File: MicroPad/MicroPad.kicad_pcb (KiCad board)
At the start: 2 copper layers, 92 x 92 mm, 69 parts, among them J10 Conn_01x02, J11 Conn_01x02, J12 Conn_01x02, J2 USB_C_Receptacle_USB2.0_16P, J4 Programming header, J5 SPI for E-Ink Display, J6 B2B-PH-K-S (Battery), J9 Conn_01x02, SW1 RESET, SW10 SWITCH, SW11 SWITCH, SW12 SWITCH, SW13 SWITCH, SW14 SWITCH, SW15 RotaryEncoder_Switch_MP, SW2 BOOT, SW3 SWITCH, SW4 SWITCH, SW5 SWITCH, SW6 SWITCH, SW7 SWITCH, SW8 SWITCH, SW9 SWITCH, U1 BQ24075RGT, U3 ESP32-S3-WROOM-1, U5 ESD7104MUTAG, U6 AP2112K-3.3

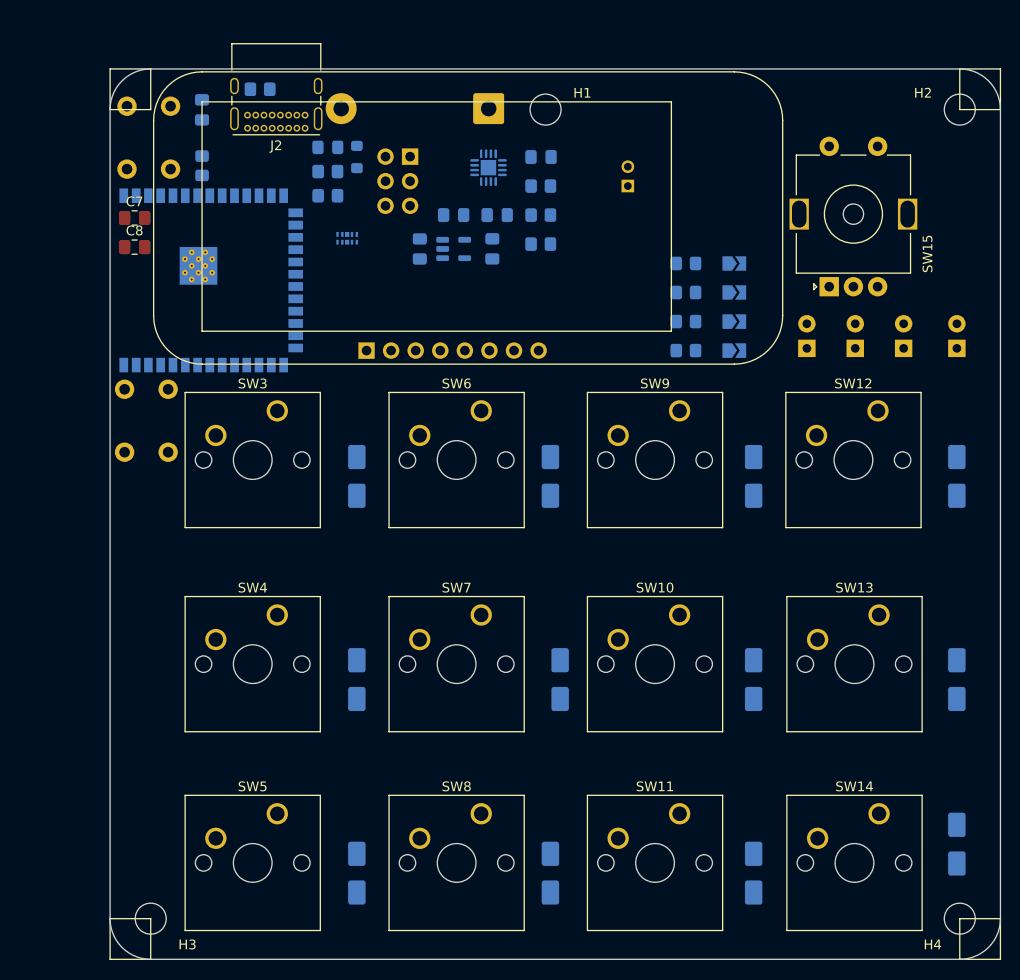
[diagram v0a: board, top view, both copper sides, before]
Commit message: new version with bigger display and one key less
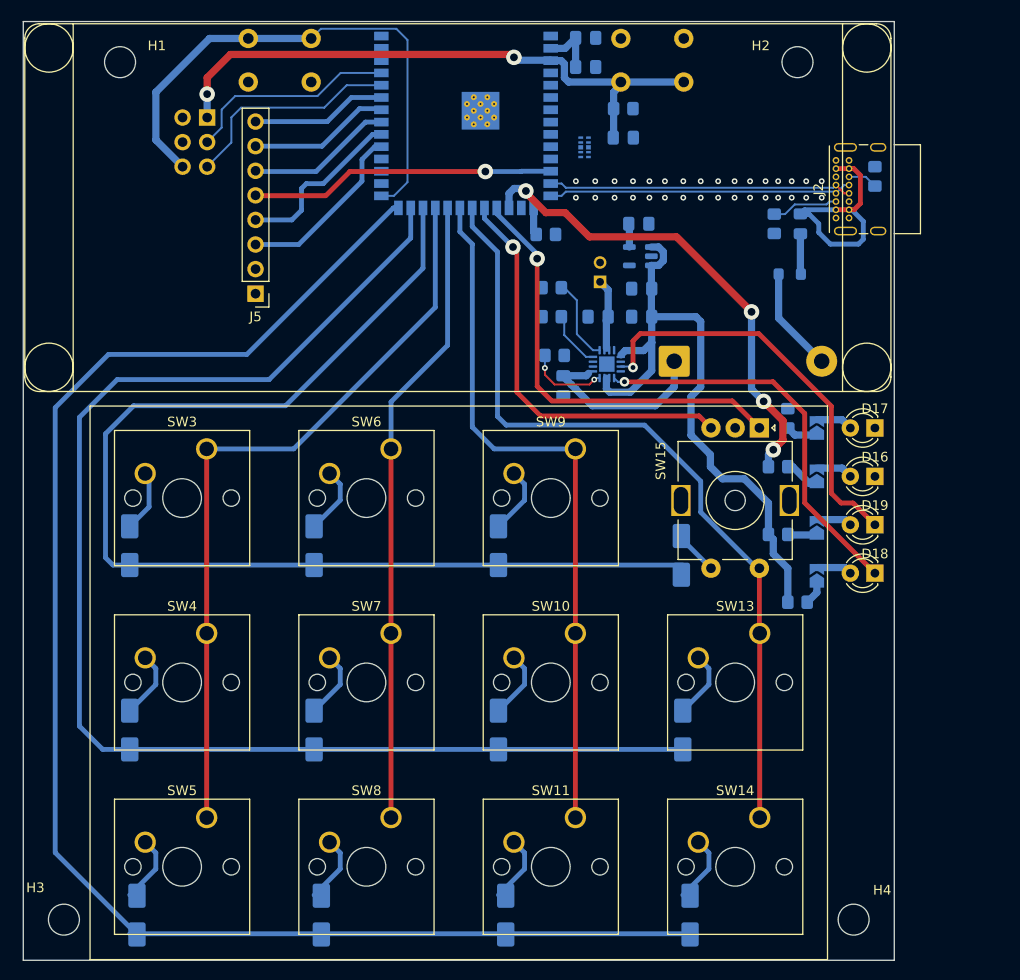
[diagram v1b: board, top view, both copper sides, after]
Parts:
- removed SW12: SWITCH, Button_Switch_Keyboard:SW_Cherry_MX_1.00u_PCB
- C7, C8: moved to B.Cu
- D16, D17, D18, D19, J5: moved to F.Cu
- moved R2 64.2 mm to (175.8, 70.0), turned to 90 degrees
- moved J2 55.6 mm to (171.7, 74.3), turned to 90 degrees
- moved SW1 54.7 mm to (156.0, 55.8), turned to 180 degrees
- moved C8 51.4 mm to (145.9, 55.7)
- moved F1 49.5 mm to (168.1, 74.9), turned to -90 degrees
- moved C7 49.1 mm to (145.9, 58.7)
- moved R1 46.4 mm to (165.3, 74.9), turned to -90 degrees
- moved FB1 46.3 mm to (166.9, 80.1), turned to 180 degrees
- moved H1 44.2 mm to (97.8, 58.2)
- moved R10 43.9 mm to (149.8, 63.0), turned to 180 degrees
- moved C9 43.6 mm to (149.8, 66.0), turned to 0 degrees
- moved U3 36.1 mm to (133.5, 60.8), turned to 180 degrees
- moved SW2 34.2 mm to (111.0, 60.2), turned to 0 degrees
- moved R14 34.0 mm to (167.8, 114.0)
- moved D1 32.4 mm to (155.0, 89.1), turned to 0 degrees
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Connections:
- D13 pad 1: Net-(D13-K) -> /S1
- SW15 pad S1: /Button -> /S1
- SW15 pad S2: GND -> /C4
- U3 pad 10: /RST -> unconnected-(U3-IO17-Pad10)
- U3 pad 11: /BUSY -> unconnected-(U3-IO18-Pad11)
- U3 pad 12: /C2 -> /CS
- U3 pad 17: /C3 -> /CTRL LED
- U3 pad 18: /C4 -> /A
- U3 pad 19: /Button -> /B
- U3 pad 20: /A -> /C4
- U3 pad 21: /B -> /C3
- U3 pad 22: /MOSI -> /C2
- U3 pad 23: /CTRL LED -> /C1
- U3 pad 24: unconnected-(U3-IO47-Pad24) -> /R1
- U3 pad 25: unconnected-(U3-IO48-Pad25) -> /R2
- U3 pad 26: unconnected-(U3-IO45-Pad26) -> /R3
- U3 pad 31: unconnected-(U3-IO38-Pad31) -> /MOSI
- U3 pad 32: unconnected-(U3-IO39-Pad32) -> /CLK
- U3 pad 33: unconnected-(U3-IO40-Pad33) -> /DC
- U3 pad 34: unconnected-(U3-IO41-Pad34) -> /RST
- U3 pad 35: unconnected-(U3-IO42-Pad35) -> /BUSY
- U3 pad 4: /R1 -> unconnected-(U3-IO4-Pad4)
- U3 pad 5: /R2 -> unconnected-(U3-IO5-Pad5)
- U3 pad 6: /R3 -> unconnected-(U3-IO6-Pad6)
- U3 pad 7: /C1 -> unconnected-(U3-IO7-Pad7)
- U3 pad 8: /CS -> unconnected-(U3-IO15-Pad8)
- U3 pad 9: /DC -> unconnected-(U3-IO16-Pad9)
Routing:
- net /R3: track 0.00 -> 159.1 mm
- net /R2: track 0.00 -> 140.3 mm
- net /R1: track 0.00 -> 118.9 mm
- net /C4: track 0.00 -> 83.8 mm
- net /C1: track 0.00 -> 78.1 mm
- net /C3: track 0.00 -> 72.9 mm
- net /C2: track 0.00 -> 65.4 mm
- net /PWR OUT: track 0.00 -> 65.4 mm
- net /EN: track 0.00 -> 62.5 mm, vias 0 -> 2
- net /BOOT: track 0.00 -> 56.0 mm
- net /CTRL LED: track 0.00 -> 50.1 mm, vias 0 -> 4
- net /A: track 0.00 -> 44.9 mm, vias 0 -> 1
- net /!PG: track 0.00 -> 42.8 mm, vias 0 -> 1
- net /B: track 0.00 -> 42.0 mm, vias 0 -> 1
- net /!CHG: track 0.00 -> 40.7 mm, vias 0 -> 1
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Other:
- board size 92 x 92 mm -> 90 x 97 mm
- copper layers 2 -> 4

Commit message: new version
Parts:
- removed U5: ESD7104MUTAG, ESD7104MUTAG:IC_ESD7104MUTAG
- added C1: 220u, Capacitor_SMD:CP_Elec_6.3x7.7, B.Cu at (160.3, 81.7)
- added C15: 100n, Capacitor_SMD:C_0805_2012Metric_Pad1.18x1.45mm_HandSolder, B.Cu at (158.6, 75.8)
- added U2: USBLC6-2SC6, Package_TO_SOT_SMD:SOT-23-6, B.Cu at (156.6, 71.1)
- moved C13 5.97 mm to (154.5, 80.0), turned to -90 degrees
- moved F1 1.52 mm to (167.6, 76.4)
- moved R1 1.42 mm to (165.0, 76.3)
- moved FB1 1.16 mm to (167.6, 81.1), turned to -90 degrees
- moved H1 1.05 mm to (96.7, 58.2)
- moved H4 0.78 mm to (172.8, 146.6)
- moved SW15 0.66 mm to (163.4, 95.5)
- moved U3 0.64 mm to (132.9, 60.5)
- moved D12 0.47 mm to (137.2, 146.1)
- moved D15 0.47 mm to (156.2, 146.1)
- moved D6 0.47 mm to (99.1, 146.1)
- moved D9 0.47 mm to (118.1, 146.1)
- moved H3 0.47 mm to (91.5, 146.6)
- moved C10 0.47 mm to (143.1, 91.4)
- moved C11 0.47 mm to (146.7, 84.3)
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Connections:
- net /S1 renamed /Diode out
- J2 pad A6: /USB_D+ -> /D+
- J2 pad A7: /USB_D- -> /D-
- J2 pad B6: /USB_D+ -> /D+
- J2 pad B7: /USB_D- -> /D-
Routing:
- net GND: track 0.00 -> 91.3 mm, vias 0 -> 40
- net VBUS: track 19.5 -> 45.1 mm, vias 0 -> 1
- net +3V3: track 8.60 -> 33.7 mm, vias 0 -> 5
- net /USB_D-: track 31.5 -> 14.5 mm
- net /USB_D+: track 31.4 -> 14.5 mm
- net /D-: track 0.00 -> 16.1 mm
- net /D+: track 0.00 -> 15.9 mm
- net Net-(D1-A): track 10.8 -> 7.58 mm
- net /EN: track 62.5 -> 64.9 mm
- net Net-(F1-Pad2): track 4.20 -> 2.50 mm
- net /CLK: track 18.0 -> 16.7 mm
- net /CS: track 31.6 -> 32.1 mm
- net Net-(F1-Pad1): track 24.8 -> 24.2 mm
- net (no net): vias 32 -> 0
- added copper zone on In2.Cu, net +3V3
- added copper zone on In1.Cu, net GND
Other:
- board size 90 x 97 mm -> 89.5 x 97 mm

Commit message: new version
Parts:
- added G***: LOGO, LOGO, F.Cu at (101.3, 79.8)
- moved J2 0.34 mm to (171.0, 74.1)
- moved U3 0.23 mm to (133.1, 60.5)
- moved H3 0.16 mm to (91.7, 146.6)
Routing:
- net GND: track 91.3 -> 93.9 mm
- net /BOOT: track 56.0 -> 53.8 mm, vias 0 -> 1
- net Net-(F1-Pad1): track 24.2 -> 23.3 mm
- net /D-: track 16.1 -> 15.3 mm
- net Net-(J2-CC1): track 7.84 -> 7.33 mm
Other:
- board size 89.5 x 97 mm -> 89.5 x 96.8 mm
- board text added: "By Jonas Lindinger"

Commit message: add: new version
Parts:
- removed SW15: RotaryEncoder_Switch_MP, Rotary_Encoder:RotaryEncoder_Alps_EC11E-Switch_Vertical_H20mm_MountingHoles
- added SW12: RotaryEncoder_Switch, Rotary_Encoder:RotaryEncoder_Alps_EC11E-Switch_Vertical_H20mm, F.Cu at (163.4, 95.5)
- moved G*** 31.0 mm to (132.3, 79.7)
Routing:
- net /R1: track 118.9 -> 103.7 mm
- net /R2: track 140.3 -> 134.8 mm
- net /R3: track 159.1 -> 157.5 mm
- net /C1: vias 0 -> 1
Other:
- outline, holes or cut-outs redrawn
